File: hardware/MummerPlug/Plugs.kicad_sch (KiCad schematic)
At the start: 8 parts

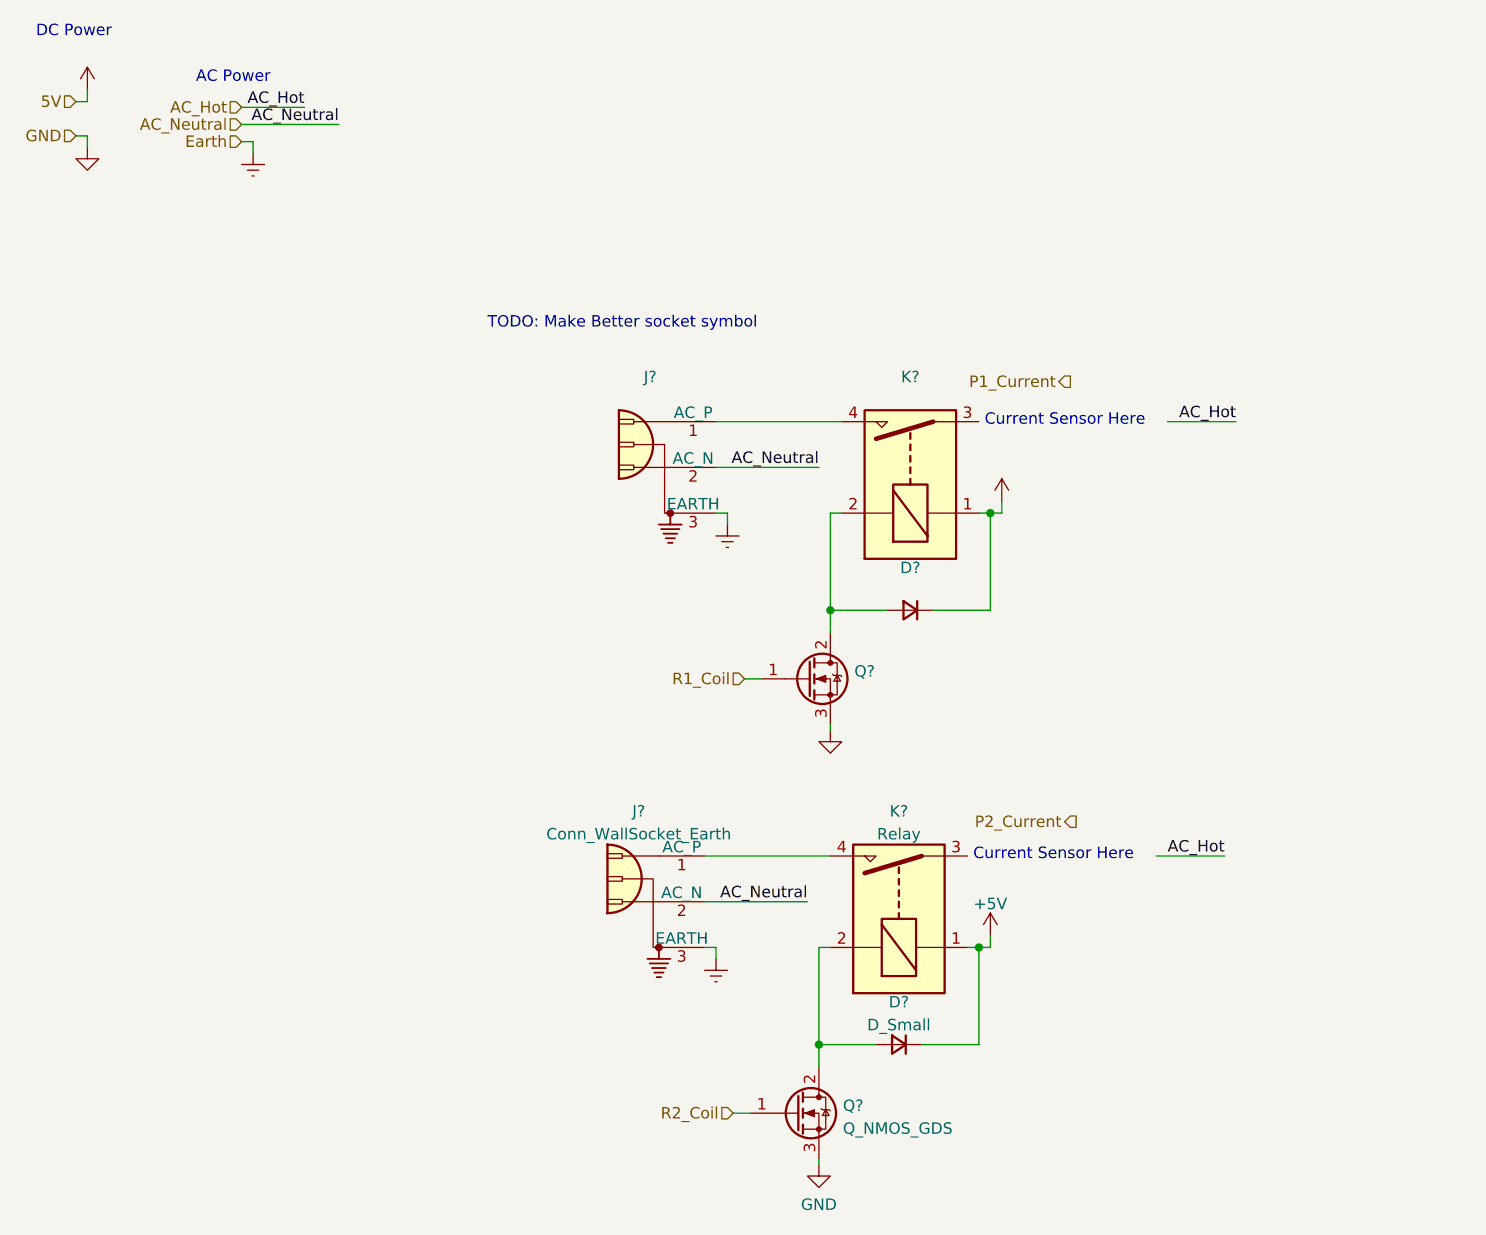
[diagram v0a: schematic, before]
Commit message: assign footprint to esp symbol
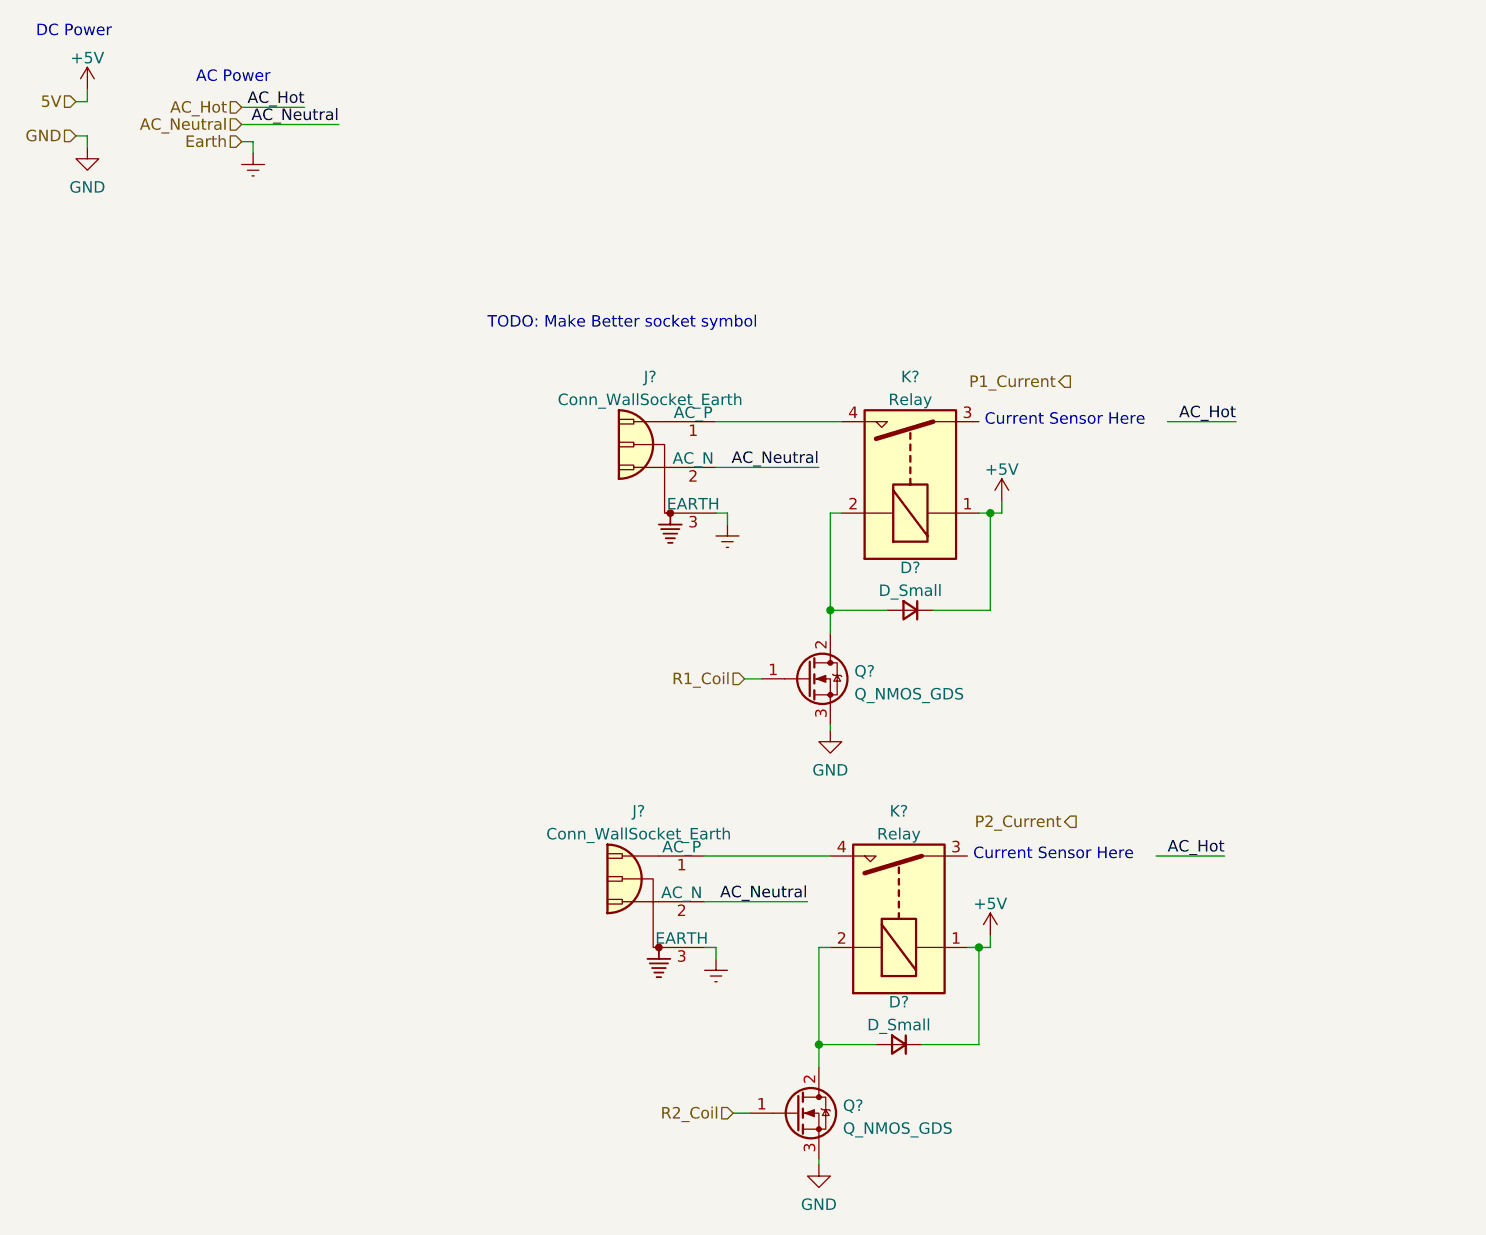
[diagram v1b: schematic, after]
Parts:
- D?: value (none) -> D_Small
- J?: value (none) -> Conn_WallSocket_Earth
- K?: value (none) -> Relay
- Q?: value (none) -> Q_NMOS_GDS
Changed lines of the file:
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@@
       (effects (font (size 1.27 1.27)) hide)
     )
-    (property "Value" "" (id 1) (at 95.25 75.565 0)
+    (property "Value" "Earth" (id 1) (at 95.25 75.565 0)
       (effects (font (size 1.27 1.27)) hide)
     )
@@
       (effects (font (size 1.27 1.27)) hide)
     )
-    (property "Value" "" (id 1) (at 42.545 34.29 0)
+    (property "Value" "Earth" (id 1) (at 42.545 34.29 0)
       (effects (font (size 1.27 1.27)) hide)
     )
@@
     (in_bom yes) (on_board yes) (fields_autoplaced)
     (property "Reference" "D?" (id 0) (at 115.57 76.5642 0))
-    (property "Value" "" (id 1) (at 115.57 79.1011 0))
+    (property "Value" "D_Small" (id 1) (at 115.57 79.1011 0))
     (property "Footprint" "" (id 2) (at 115.57 81.28 90)
       (effects (font (size 1.27 1.27)) hide)
@@
       (effects (font (size 1.27 1.27)) hide)
     )
-    (property "Value" "" (id 1) (at 24.13 34.2884 0))
+    (property "Value" "GND" (id 1) (at 24.13 34.2884 0))
     (property "Footprint" "" (id 2) (at 24.13 29.845 0)
       (effects (font (size 1.27 1.27)) hide)
@@
       (effects (font (size 1.27 1.27)) hide)
     )
-    (property "Value" "" (id 1) (at 106.68 99.0584 0))
+    (property "Value" "GND" (id 1) (at 106.68 99.0584 0))
     (property "Footprint" "" (id 2) (at 106.68 94.615 0)
       (effects (font (size 1.27 1.27)) hide)
@@
       (effects (font (size 1.27 1.27)) hide)
     )
-    (property "Value" "" (id 1) (at 24.13 19.9192 0))
+    (property "Value" "+5V" (id 1) (at 24.13 19.9192 0))
     (property "Footprint" "" (id 2) (at 24.13 23.495 0)
       (effects (font (size 1.27 1.27)) hide)
@@
     (in_bom yes) (on_board yes) (fields_autoplaced)
     (property "Reference" "K?" (id 0) (at 115.57 55.3552 90))
-    (property "Value" "" (id 1) (at 115.57 57.8921 90))
+    (property "Value" "Relay" (id 1) (at 115.57 57.8921 90))
     (property "Footprint" "" (id 2) (at 116.84 57.785 0)
       (effects (font (size 1.27 1.27)) (justify left) hide)
@@
       (effects (font (size 1.27 1.27)) hide)
     )
-    (property "Value" "" (id 1) (at 125.73 65.6392 0))
+    (property "Value" "+5V" (id 1) (at 125.73 65.6392 0))
     (property "Footprint" "" (id 2) (at 125.73 69.215 0)
       (effects (font (size 1.27 1.27)) hide)
@@
       (effects (font (size 1.27 1.27)) (justify left))
     )
-    (property "Value" "" (id 1) (at 109.347 90.6022 0)
+    (property "Value" "Q_NMOS_GDS" (id 1) (at 109.347 90.6022 0)
       (effects (font (size 1.27 1.27)) (justify left))
     )
@@
     (in_bom yes) (on_board yes) (fields_autoplaced)
     (property "Reference" "J?" (id 0) (at 86.6648 55.3552 0))
-    (property "Value" "" (id 1) (at 86.6648 57.8921 0))
+    (property "Value" "Conn_WallSocket_Earth" (id 1) (at 86.6648 57.8921 0))
     (property "Footprint" "" (id 2) (at 96.52 62.865 0)
       (effects (font (size 1.27 1.27)) hide)

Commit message: current sensor footprint and insert into schematic
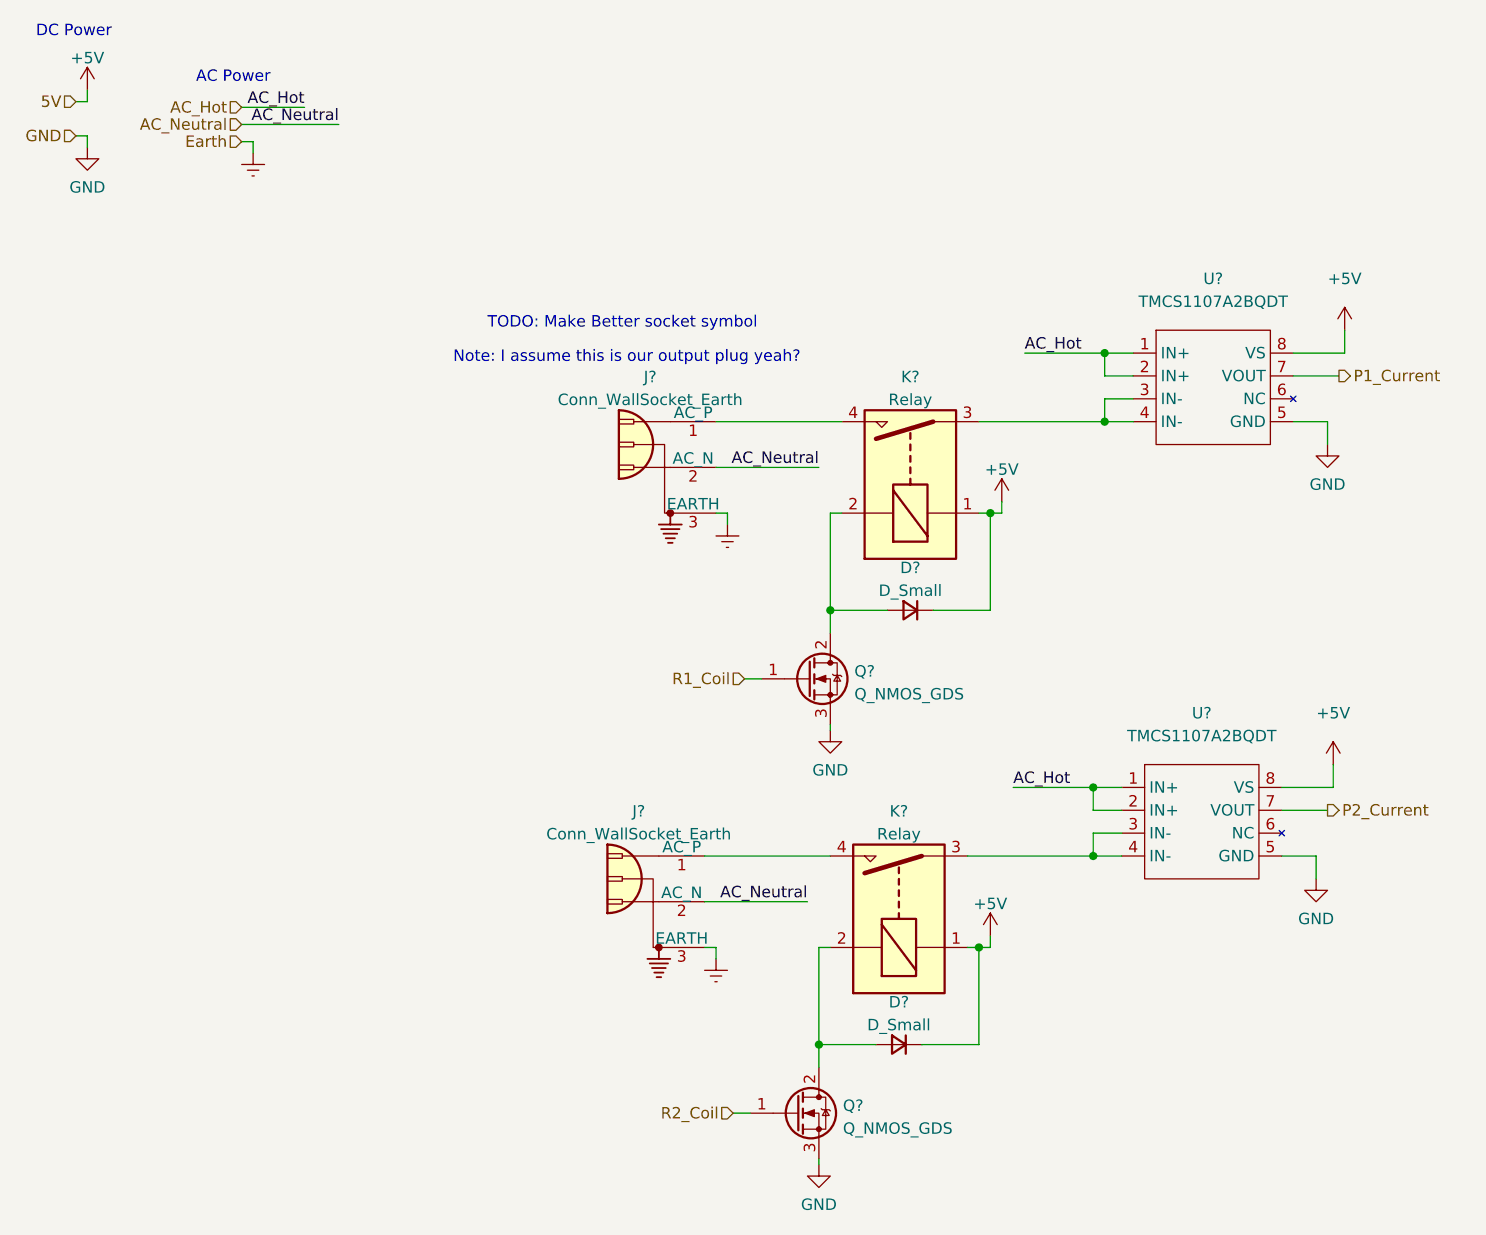
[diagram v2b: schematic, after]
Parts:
- added U? (x2): TMCS1107A2BQDT, mummerplug:TMCS1107A2BQDT, symbol Mummerplug:TMCS1107A2BQDT
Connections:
- net +5V: now also U?.8 (VS), U?.8 (VS)
- net AC_Hot: now also U?.1 (IN+), U?.1 (IN+), U?.2 (IN+), U?.2 (IN+)
- net GND: now also U?.5 (GND), U?.5 (GND)
- net P1_Current: now also U?.7 (VOUT)
- net P2_Current: now also U?.7 (VOUT)
- net at K?.3: now also U?.3 (IN-), U?.4 (IN-) (x2)
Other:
- note added: "Note: I assume this is our output plug yeah?"
- note removed: "Current Sensor Here"
